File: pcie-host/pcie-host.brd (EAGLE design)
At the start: 167.6 x 111.2 mm, 228 parts, among them Q1 BSH103, Q2 BSH103, Q3 NDS351AN, Q4 NDS351AN, Q5 NDS351AN, U100 UEI15-050-Q12P-C, U104 ISO7240M, U105 ISO7240M, U106 ISO7240M, U107 ISO7240M

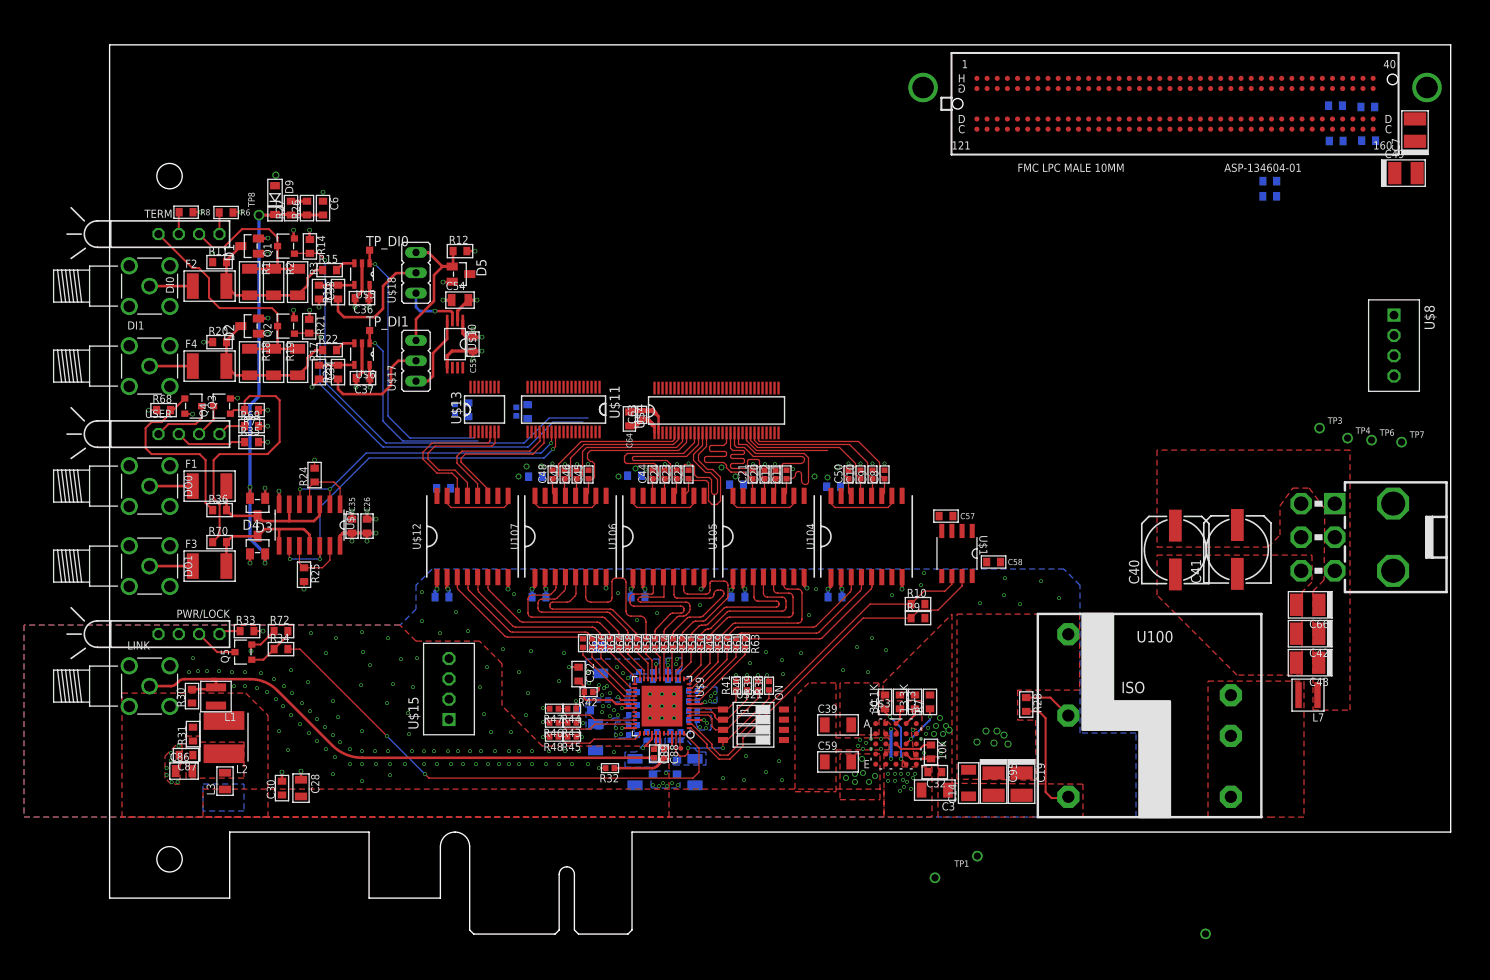
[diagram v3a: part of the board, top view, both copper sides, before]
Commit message: More PCIe host layout.
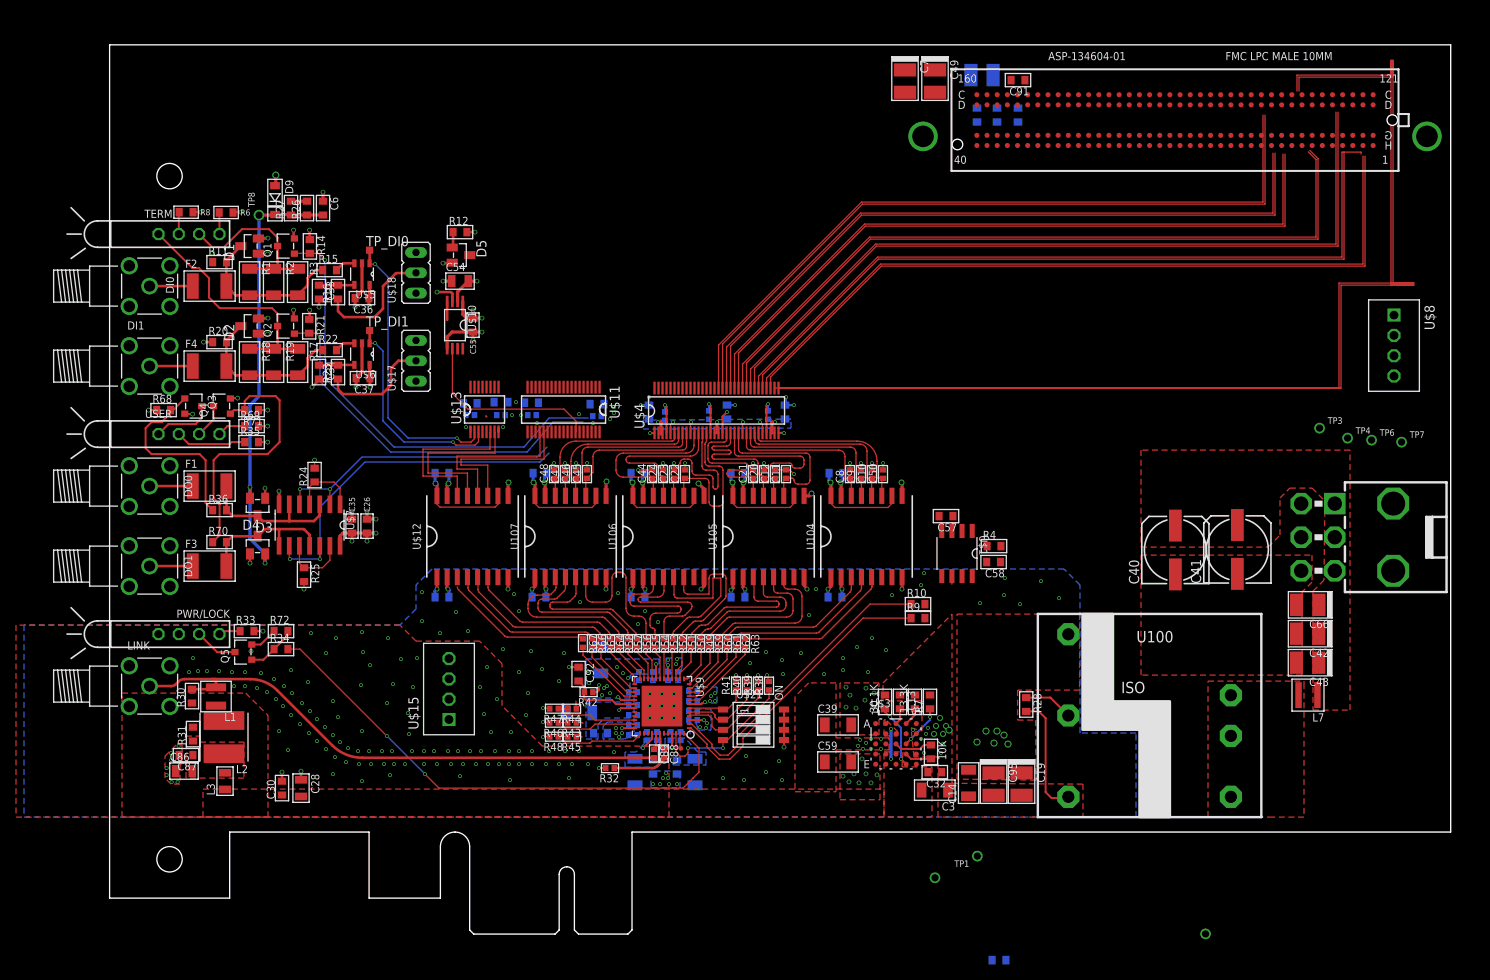
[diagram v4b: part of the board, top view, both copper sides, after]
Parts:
- added C51, C53, C61, C65: 1nF, jonnew:0402
- added C52, C56, C62, C90: 100nF, RHD2000_eval_board:0603
- added C91: 100nF, jonnew:0603
- C25, C29, C31, C57, C58: device RHD2000_eval_board:0603 -> jonnew:0603
- C27: value 100nF -> 22uF; device RHD2000_eval_board:0603 -> jonnew:1210-POL
- R36, R70: value 1k -> 4.7k
- U$12: value (none) -> ISO7242M
- moved R5 103.1 mm to (111.4, -7.88)
- moved C7 64.0 mm to (99.6, 102.0), turned to 270 degrees
- moved C49 60.0 mm to (103.4, 102.0), turned to 270 degrees
- moved R4 55.7 mm to (110.8, 43.9), flipped to the top
- moved C27 48.4 mm to (109.2, 102.8)
- moved C29 44.8 mm to (108.6, 97.8), turned to 270 degrees
- moved C25 43.9 mm to (113.8, 97.8), turned to 90 degrees
- moved C31 42.5 mm to (111.1, 97.8), turned to 90 degrees
- moved C8 4.32 mm to (92.8, 52.9)
- moved C50 4.31 mm to (96.9, 52.9)
- moved C80 3.69 mm to (58.9, 23.1), turned to 180 degrees
- moved L5 3.56 mm to (61.6, 20.5), turned to 180 degrees
- moved C63 2.87 mm to (69.6, 60.1), flipped to the bottom, turned to 270 degrees
- moved C64 2.59 mm to (67.6, 60.6), flipped to the bottom, turned to 270 degrees
- moved C54 2.38 mm to (44.0, 77.0)
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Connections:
- removed net 12V_FPGA: C49.+, C7.+, TP6.1, U$14.P$155, U$14.P$157, U$8.P$3
- removed net N$100: U$14.P$55
- removed net N$101: U$14.P$53
- removed net N$102: U$14.P$52
- removed net N$103: U$14.P$50
- removed net N$104: U$14.P$49
- removed net N$105: U$14.P$47
- removed net N$106: U$14.P$46
- removed net N$107: U$14.P$88
- removed net N$108: U$14.P$89
- removed net N$109: U$14.P$91
- removed net N$110: U$14.P$92
- removed net N$111: U$14.P$94
- removed net N$112: U$14.P$95
- removed net N$113: U$14.P$97
- removed net N$114: U$14.P$98
- removed net N$115: U$14.P$100
- removed net N$116: U$14.P$101
- removed net N$117: U$14.P$103
- removed net N$118: U$14.P$104
- removed net N$119: U$14.P$106
- removed net N$120: U$14.P$107
- removed net N$121: U$14.P$130
- removed net N$122: U$14.P$131
- removed net N$123: U$14.P$134
- removed net N$124: U$14.P$135
- removed net N$125: U$14.P$138
- removed net N$126: U$14.P$139
- removed net N$127: U$14.P$142
- removed net N$128: U$14.P$143
- removed net N$129: U$14.P$146
- removed net N$130: U$14.P$147
- removed net N$37: U$14.P$7
- removed net N$63: U$14.P$8
- removed net N$65: U$14.P$10
- removed net N$66: U$14.P$11
- removed net N$67: U$14.P$13
- removed net N$68: U$14.P$14
- removed net N$69: U$14.P$16
- removed net N$70: U$14.P$17
- removed net N$71: U$14.P$19
- removed net N$72: U$14.P$20
- removed net N$73: U$14.P$22
- removed net N$74: U$14.P$23
- removed net N$75: U$14.P$25
- removed net N$76: U$14.P$26
- removed net N$77: U$14.P$28
- removed net N$78: U$14.P$29
- removed net N$79: U$14.P$31
- removed net N$80: U$14.P$32
- removed net N$81: U$14.P$34
- removed net N$82: U$14.P$35
- removed net N$83: U$14.P$37
- removed net N$84: U$14.P$38
- removed net N$85: U$14.P$77
- removed net N$86: U$14.P$76
- removed net N$87: U$14.P$74
- removed net N$88: U$14.P$73
- removed net N$89: U$14.P$71
- removed net N$90: U$14.P$70
- removed net N$91: U$14.P$68
- removed net N$92: U$14.P$67
- removed net N$93: U$14.P$65
- removed net N$94: U$14.P$64
- removed net N$95: U$14.P$62
- removed net N$96: U$14.P$61
- removed net N$97: U$14.P$59
- removed net N$98: U$14.P$58
- removed net N$99: U$14.P$56
- new net +3V3_ISO_PG_N: U$14.P$89, U$4.33
- new net +3V3_ISO_PG_P: U$14.P$88, U$4.34
- new net D10_N: U$14.P$50, U$4.43
- new net D10_P: U$14.P$49, U$4.44
- new net D11_N: U$14.P$8, U$4.41
- new net D11_P: U$14.P$7, U$4.42
- new net D1_N: U$4.61
- new net D1_P: U$4.62
- new net D2_N: U$4.59
- new net D2_P: U$4.60
- new net D3_N: U$4.57
- new net D3_P: U$4.58
- new net D4_N: U$4.55
- new net D4_P: U$4.56
- new net D5_N: U$4.53
- new net D5_P: U$4.54
- new net D6_N: U$4.51
- new net D6_P: U$4.52
- new net D7_N: U$4.49
- new net D7_P: U$4.50
- new net D8_N: U$14.P$92, U$4.47
- new net D8_P: U$14.P$91, U$4.48
- new net D9_N: U$14.P$11, U$4.45
- new net D9_P: U$14.P$10, U$4.46
- new net DO_N: U$4.63
- new net DO_P: U$4.64
- new net HSYNC_N: U$14.P$85, U$4.39
- new net HSYNC_P: U$14.P$84, U$4.40
- new net PCLK_N: U$14.P$43, U$4.35
- new net PCLK_P: U$14.P$42, U$4.36
- new net VSYNC_N: U$14.P$5, U$4.37
- new net VSYNC_P: U$14.P$4, U$4.38
- net +12V_FPGA: now also C49.+, C7.+, C91.2, TP6.1, U$14.P$155, U$14.P$157, U$8.P$3
- net +3V3: now also C27.+, C51.2, C52.2, C53.2, C56.2, C61.2, C62.2, C65.2, C90.2; no longer C27.2
- net +3V3_ISO_PG: now also U$4.27, U104.P11; no longer U$4.24, U104.P14
- net D0: now also C48.1, U$4.6, U107.P14; no longer C45.1, U$4.9, U107.P11
- net D1: now also C47.1, U$4.7, U107.P13; no longer C46.1, U$4.8, U107.P12
- net D10: now also C12.1, U$4.21, U105.P12; no longer C20.1, U$4.20, U105.P13
- net D11: now also C11.1, U$4.22, U105.P11; no longer C21.1, U$4.19, U105.P14
- net D2: now also C46.1, U$4.8, U107.P12; no longer C47.1, U$4.7, U107.P13
- net D3: now also C45.1, U$4.9, U107.P11; no longer C48.1, U$4.6, U107.P14
- net D4: now also C44.1, U$4.11, U106.P14; no longer C22.1, U$4.14, U106.P11
- net D5: now also C24.1, U$4.12, U106.P13; no longer C23.1, U$4.13, U106.P12
- net D6: now also C23.1, U$4.13, U106.P12; no longer C24.1, U$4.12, U106.P13
- net D7: now also C22.1, U$4.14, U106.P11; no longer C44.1, U$4.11, U106.P14
- net D8: now also C21.1, U$4.19, U105.P14; no longer C11.1, U$4.22, U105.P11
- net D9: now also C20.1, U$4.20, U105.P13; no longer C12.1, U$4.21, U105.P12
- net GND: now also C27.-, C51.1, C52.1, C53.1, C56.1, C61.1, C62.1, C65.1, C90.1, C91.1; no longer C27.1
- net GPI0_ISO: now also R67.1, U$12.P3; no longer R65.1, U$12.P5
- net GPI1_ISO: now also R66.1, U$12.P4; no longer R64.1, U$12.P6
- net GPO0_ISO: now also R65.1, U$12.P5; no longer R67.1, U$12.P3
- net GPO1_ISO: now also R64.1, U$12.P6; no longer R66.1, U$12.P4
- net HSYNC: now also U$4.24, U104.P14; no longer U$4.27, U104.P11
- net PCLK: now also U$4.26, U104.P12; no longer U$4.25, U104.P13
- net VSYNC: now also U$4.25, U104.P13; no longer U$4.26, U104.P12
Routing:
- net +3V3_ISO_PG_P: track 0.00 -> 139.7 mm
- net +3V3_ISO_PG_N: track 0.00 -> 138.4 mm
- net HSYNC_P: track 0.00 -> 98.5 mm
- net HSYNC_N: track 0.00 -> 98.5 mm
- net VSYNC_P: track 0.00 -> 96.3 mm
- net PCLK_P: track 0.00 -> 95.2 mm
- net PCLK_N: track 0.00 -> 95.2 mm
- net VSYNC_N: track 0.00 -> 93.7 mm
- net D11_N: track 0.00 -> 92.5 mm
- net D11_P: track 0.00 -> 92.3 mm
- net D8_P: track 0.00 -> 91.7 mm
- net D8_N: track 0.00 -> 91.7 mm
- net D10_P: track 0.00 -> 88.3 mm
- net D10_N: track 0.00 -> 88.3 mm
- net D9_P: track 0.00 -> 87.9 mm
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- added copper zone on layer 15, net +1V8_ISO
- added copper zone on layer 16, net +3V3
- removed copper zone on layer 16, net +12V_ISO

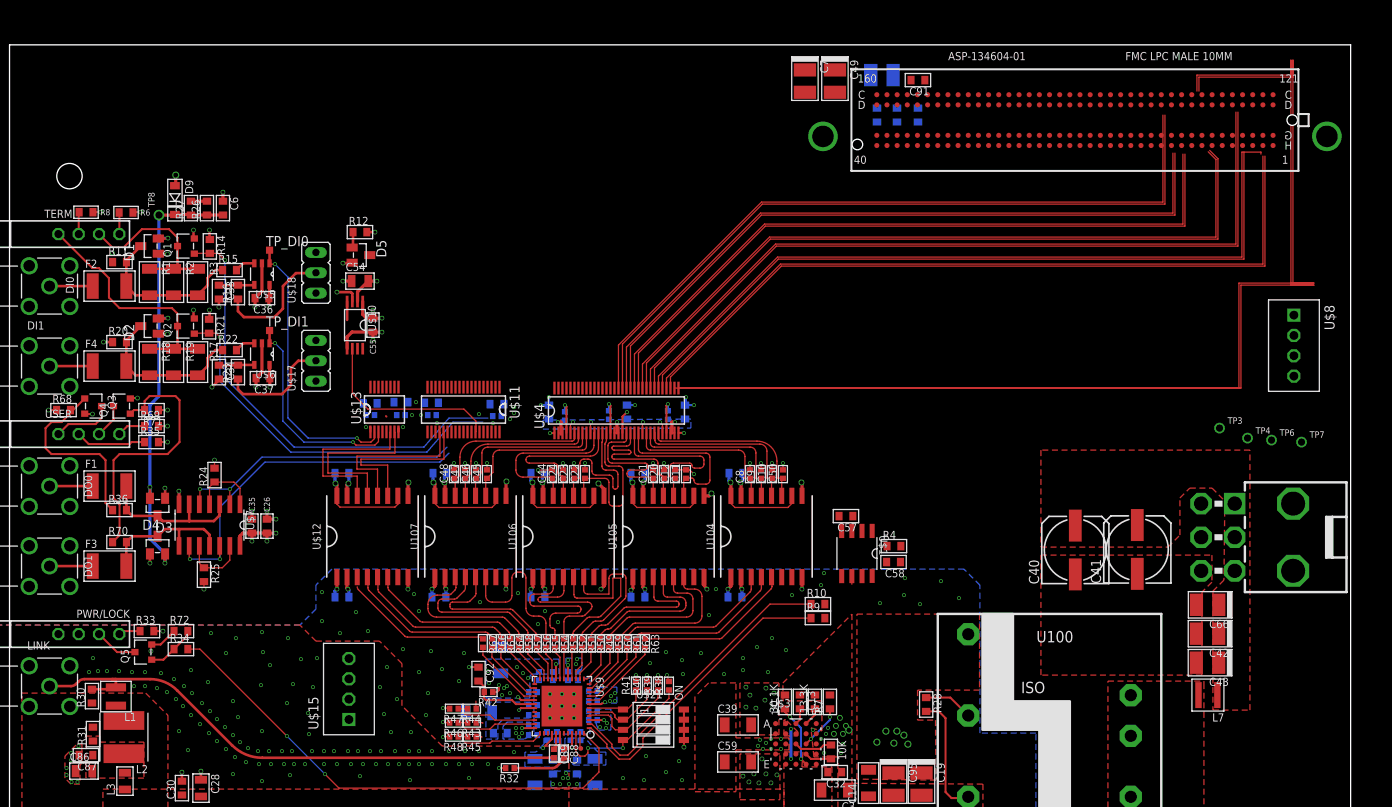
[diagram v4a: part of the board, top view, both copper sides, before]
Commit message: Nearly finished with PCIe host routing.
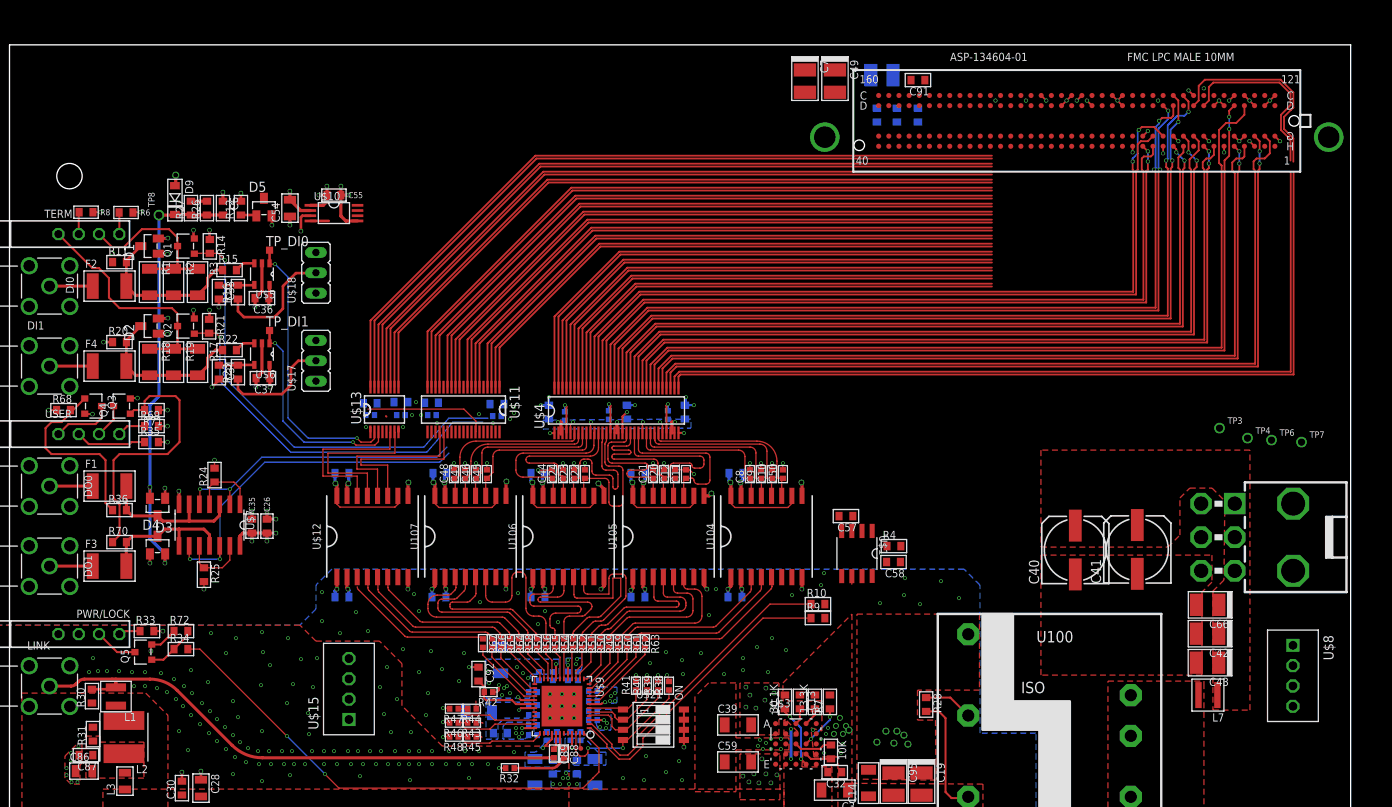
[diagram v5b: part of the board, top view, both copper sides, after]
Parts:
- U$11: value SN65LVDS388A -> SN65LVDT388A
- moved U$8 41.3 mm to (160.6, 31.5)
- moved C55 17.0 mm to (40.8, 87.8), turned to 180 degrees
- moved R12 15.2 mm to (29.1, 86.1), turned to 90 degrees
- moved U$10 14.2 mm to (40.8, 85.5), turned to 270 degrees
- moved D5 13.5 mm to (32.0, 86.2), turned to 0 degrees
- moved C54 12.6 mm to (35.2, 86.1), turned to 90 degrees
- moved U$14 0.25 mm to (133.6, 97.0)
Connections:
- removed net DAC_LAT+: U$11.6
- removed net DAC_LAT-: U$11.7
- removed net DI0+: U$13.16
- removed net DI0_TERM+: U$11.1
- removed net DI0_TERM-: U$11.2
- removed net DI1+: U$13.14
- removed net DI1-: U$13.13
- removed net DI1_TERM+: U$11.3
- removed net DI1_TERM-: U$11.4
- removed net DIO-: U$13.15
- removed net DO0+: U$11.11
- removed net DO0-: U$11.12
- removed net DO1+: U$11.13
- removed net DO1-: U$11.14
- removed net DO_TEST+: U$11.8
- removed net DO_TEST-: U$11.9
- removed net GPI0+: U$13.12
- removed net GPI0-: U$13.11
- removed net GPI1+: U$13.10
- removed net GPI1-: U$13.9
- removed net GPO0+: U$11.16
- removed net GPO0-: U$11.17
- removed net GPO1+: U$11.18
- removed net GPO1-: U$11.19
- new net DAC_LAT_N: U$11.7, U$14.P$59
- new net DAC_LAT_P: U$11.6, U$14.P$58
- new net DI0_N: U$13.15, U$14.P$68
- new net DI0_P: U$13.16, U$14.P$67
- new net DI0_TERM_N: U$11.2, U$14.P$139
- new net DI0_TERM_P: U$11.1, U$14.P$138
- new net DI1_N: U$13.13, U$14.P$29
- new net DI1_P: U$13.14, U$14.P$28
- new net DI1_TERM_N: U$11.4, U$14.P$20
- new net DI1_TERM_P: U$11.3, U$14.P$19
- new net DO0_N: U$11.12, U$14.P$143
- new net DO0_P: U$11.11, U$14.P$142
- new net DO1_N: U$11.14, U$14.P$23
- new net DO1_P: U$11.13, U$14.P$22
- new net DO_TEST_N: U$11.9, U$14.P$101
- new net DO_TEST_P: U$11.8, U$14.P$100
- new net GPI0_N: U$13.9, U$14.P$65
- new net GPI0_P: U$13.10, U$14.P$64
- new net GPI1_N: U$13.11, U$14.P$104
- new net GPI1_P: U$13.12, U$14.P$103
- new net GPO0_N: U$11.17, U$14.P$62
- new net GPO0_P: U$11.16, U$14.P$61
- new net GPO1_N: U$11.19, U$14.P$26
- new net GPO1_P: U$11.18, U$14.P$25
- net D1_N: now also U$14.P$56
- net D1_P: now also U$14.P$55
- net D2_N: now also U$14.P$17
- net D2_P: now also U$14.P$16
- net D3_N: now also U$14.P$135
- net D3_P: now also U$14.P$134
- net D4_N: now also U$14.P$95
- net D4_P: now also U$14.P$94
- net D5_N: now also U$14.P$53
- net D5_P: now also U$14.P$52
- net D6_N: now also U$14.P$14
- net D6_P: now also U$14.P$13
- net D7_N: now also U$14.P$92
- net D7_P: now also U$14.P$91
- net D8_N: now also U$14.P$131; no longer U$14.P$92
- net D8_P: now also U$14.P$130; no longer U$14.P$91
- net DO_N: now also U$14.P$98
- net DO_P: now also U$14.P$97
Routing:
- net D7_P: track 0.00 -> 102.5 mm, vias 0 -> 2
- net D7_N: track 0.00 -> 101.7 mm, vias 0 -> 2
- net D5_P: track 0.00 -> 100.3 mm, vias 0 -> 2
- net D5_N: track 0.00 -> 97.0 mm
- net D6_P: track 0.00 -> 96.0 mm
- net D6_N: track 0.00 -> 95.3 mm, vias 0 -> 2
- net DI0_P: track 0.00 -> 94.5 mm
- net DI0_N: track 0.00 -> 93.9 mm
- net DI1_P: track 0.00 -> 92.8 mm
- net DI1_N: track 0.00 -> 92.2 mm
- net GPI1_P: track 0.00 -> 91.1 mm
- net GPI1_N: track 0.00 -> 90.5 mm
- net GPI0_P: track 0.00 -> 89.4 mm
- net GPI0_N: track 0.00 -> 88.8 mm
- net GPO1_N: track 0.00 -> 85.0 mm
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- added copper zone on layer 15, net GND
